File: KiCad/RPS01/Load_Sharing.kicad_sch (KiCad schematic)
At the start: 5 parts, among them U2 LTC4416EMS-1-TRPBF, U3 NP100P04PLG-E1-AY, U4 NP100P04PLG-E1-AY, U5 NP100P04PLG-E1-AY, U6 NP100P04PLG-E1-AY

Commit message: Updates
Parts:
- U2: footprint Mechatronic Footprints:MSOP-10_MS_LIT -> LTC4416:MSOP-10_MS_LIT
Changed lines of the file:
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@@
       (effects (font (size 1.524 1.524)))
     )
-    (property "Footprint" "Mechatronic Footprints:MSOP-10_MS_LIT" (at 91.44 119.38 0)
+    (property "Footprint" "LTC4416:MSOP-10_MS_LIT" (at 91.44 119.38 0)
       (effects (font (size 1.27 1.27) italic) hide)
     )

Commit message: Changed footprints on my end only
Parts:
- U2: footprint LTC4416:MSOP-10_MS_LIT -> Mechatronics LTC4416:MSOP-10_MS_LIT
- U3, U4, U5, U6: footprint Mechatronic Footprints:PRSS0004AL-A_REN -> Mechatronics LTC3780:PRSS0004AL-A_REN
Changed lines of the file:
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@@
       (effects (font (size 1.524 1.524)))
     )
-    (property "Footprint" "Mechatronic Footprints:PRSS0004AL-A_REN" (at 154.94 78.74 0)
+    (property "Footprint" "Mechatronics LTC3780:PRSS0004AL-A_REN" (at 154.94 78.74 0)
       (effects (font (size 1.27 1.27) italic) hide)
     )
@@
       (effects (font (size 1.524 1.524)))
     )
-    (property "Footprint" "LTC4416:MSOP-10_MS_LIT" (at 91.44 119.38 0)
+    (property "Footprint" "Mechatronics LTC4416:MSOP-10_MS_LIT" (at 91.44 119.38 0)
       (effects (font (size 1.27 1.27) italic) hide)
     )
@@
       (effects (font (size 1.524 1.524)))
     )
-    (property "Footprint" "Mechatronic Footprints:PRSS0004AL-A_REN" (at 154.94 50.8 0)
+    (property "Footprint" "Mechatronics LTC3780:PRSS0004AL-A_REN" (at 154.94 50.8 0)
       (effects (font (size 1.27 1.27) italic) hide)
     )
@@
       (effects (font (size 1.524 1.524)))
     )
-    (property "Footprint" "Mechatronic Footprints:PRSS0004AL-A_REN" (at 154.94 156.21 0)
+    (property "Footprint" "Mechatronics LTC3780:PRSS0004AL-A_REN" (at 154.94 156.21 0)
       (effects (font (size 1.27 1.27) italic) hide)
     )
@@
       (effects (font (size 1.524 1.524)))
     )
-    (property "Footprint" "Mechatronic Footprints:PRSS0004AL-A_REN" (at 154.94 130.81 0)
+    (property "Footprint" "Mechatronics LTC3780:PRSS0004AL-A_REN" (at 154.94 130.81 0)
       (effects (font (size 1.27 1.27) italic) hide)
     )

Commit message: All Footprints Load from Mechatronics Folder
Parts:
- U2: footprint Mechatronics LTC4416:MSOP-10_MS_LIT -> Mechatronic Footprints:LTC4416_MSOP-10_MS_LIT
- U3, U4, U5, U6: footprint Mechatronics LTC3780:PRSS0004AL-A_REN -> Mechatronic Footprints:LTC3780_PRSS0004AL-A_REN
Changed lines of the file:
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@@
       (effects (font (size 1.524 1.524)))
     )
-    (property "Footprint" "Mechatronics LTC3780:PRSS0004AL-A_REN" (at 154.94 78.74 0)
+    (property "Footprint" "Mechatronic Footprints:LTC3780_PRSS0004AL-A_REN" (at 154.94 78.74 0)
       (effects (font (size 1.27 1.27) italic) hide)
     )
@@
       (effects (font (size 1.524 1.524)))
     )
-    (property "Footprint" "Mechatronics LTC4416:MSOP-10_MS_LIT" (at 91.44 119.38 0)
+    (property "Footprint" "Mechatronic Footprints:LTC4416_MSOP-10_MS_LIT" (at 91.44 119.38 0)
       (effects (font (size 1.27 1.27) italic) hide)
     )
@@
       (effects (font (size 1.524 1.524)))
     )
-    (property "Footprint" "Mechatronics LTC3780:PRSS0004AL-A_REN" (at 154.94 50.8 0)
+    (property "Footprint" "Mechatronic Footprints:LTC3780_PRSS0004AL-A_REN" (at 154.94 50.8 0)
       (effects (font (size 1.27 1.27) italic) hide)
     )
@@
       (effects (font (size 1.524 1.524)))
     )
-    (property "Footprint" "Mechatronics LTC3780:PRSS0004AL-A_REN" (at 154.94 156.21 0)
+    (property "Footprint" "Mechatronic Footprints:LTC3780_PRSS0004AL-A_REN" (at 154.94 156.21 0)
       (effects (font (size 1.27 1.27) italic) hide)
     )
@@
       (effects (font (size 1.524 1.524)))
     )
-    (property "Footprint" "Mechatronics LTC3780:PRSS0004AL-A_REN" (at 154.94 130.81 0)
+    (property "Footprint" "Mechatronic Footprints:LTC3780_PRSS0004AL-A_REN" (at 154.94 130.81 0)
       (effects (font (size 1.27 1.27) italic) hide)
     )

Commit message: adjustments to main board revision
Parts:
- added U13, U8: NP100P04PLG-E1-AY, Mechatronic Footprints:LTC3780_PRSS0004AL-A_REN, symbol 2023-03-29_08-56-31:NP100P04PLG-E1-AY
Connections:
- net G1: now also U13.1 (GATE)
- net G2: now also U8.1 (GATE)
- net Vin1: now also U13.2 (DRAIN), U13.4 (FIN)
- net Vin2: now also U8.2 (DRAIN), U8.4 (FIN)
- net Vout: now also U13.3 (SOURCE), U8.3 (SOURCE)
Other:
- moved on the sheet: U2, U3, U4, U5, U6

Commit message: Updates
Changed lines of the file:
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@@
     (effects (font (size 1.27 1.27)) (justify left bottom))
   )
-  (label "VS" (at 157.48 104.14 0) (fields_autoplaced)
+  (label "+BATT" (at 157.48 104.14 0) (fields_autoplaced)
     (effects (font (size 1.27 1.27)) (justify left bottom))
   )

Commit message: Large Schematic Update
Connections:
- net Vin1 renamed VIN1
- net Vin2 renamed VIN2
- net Vout renamed VOUT
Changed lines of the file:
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@@
     (effects (font (size 1.27 1.27)) (justify left bottom))
   )
-  (hierarchical_label "Vout" (shape input) (at 167.64 104.14 0) (fields_autoplaced)
+  (hierarchical_label "VOUT" (shape input) (at 167.64 104.14 0) (fields_autoplaced)
     (effects (font (size 1.27 1.27)) (justify left))
   )
-  (hierarchical_label "Vin1" (shape input) (at 24.13 95.25 180) (fields_autoplaced)
+  (hierarchical_label "VIN1" (shape input) (at 24.13 95.25 180) (fields_autoplaced)
     (effects (font (size 1.27 1.27)) (justify right))
   )
-  (hierarchical_label "Vin2" (shape input) (at 22.86 111.76 180) (fields_autoplaced)
+  (hierarchical_label "VIN2" (shape input) (at 22.86 111.76 180) (fields_autoplaced)
     (effects (font (size 1.27 1.27)) (justify right))
   )

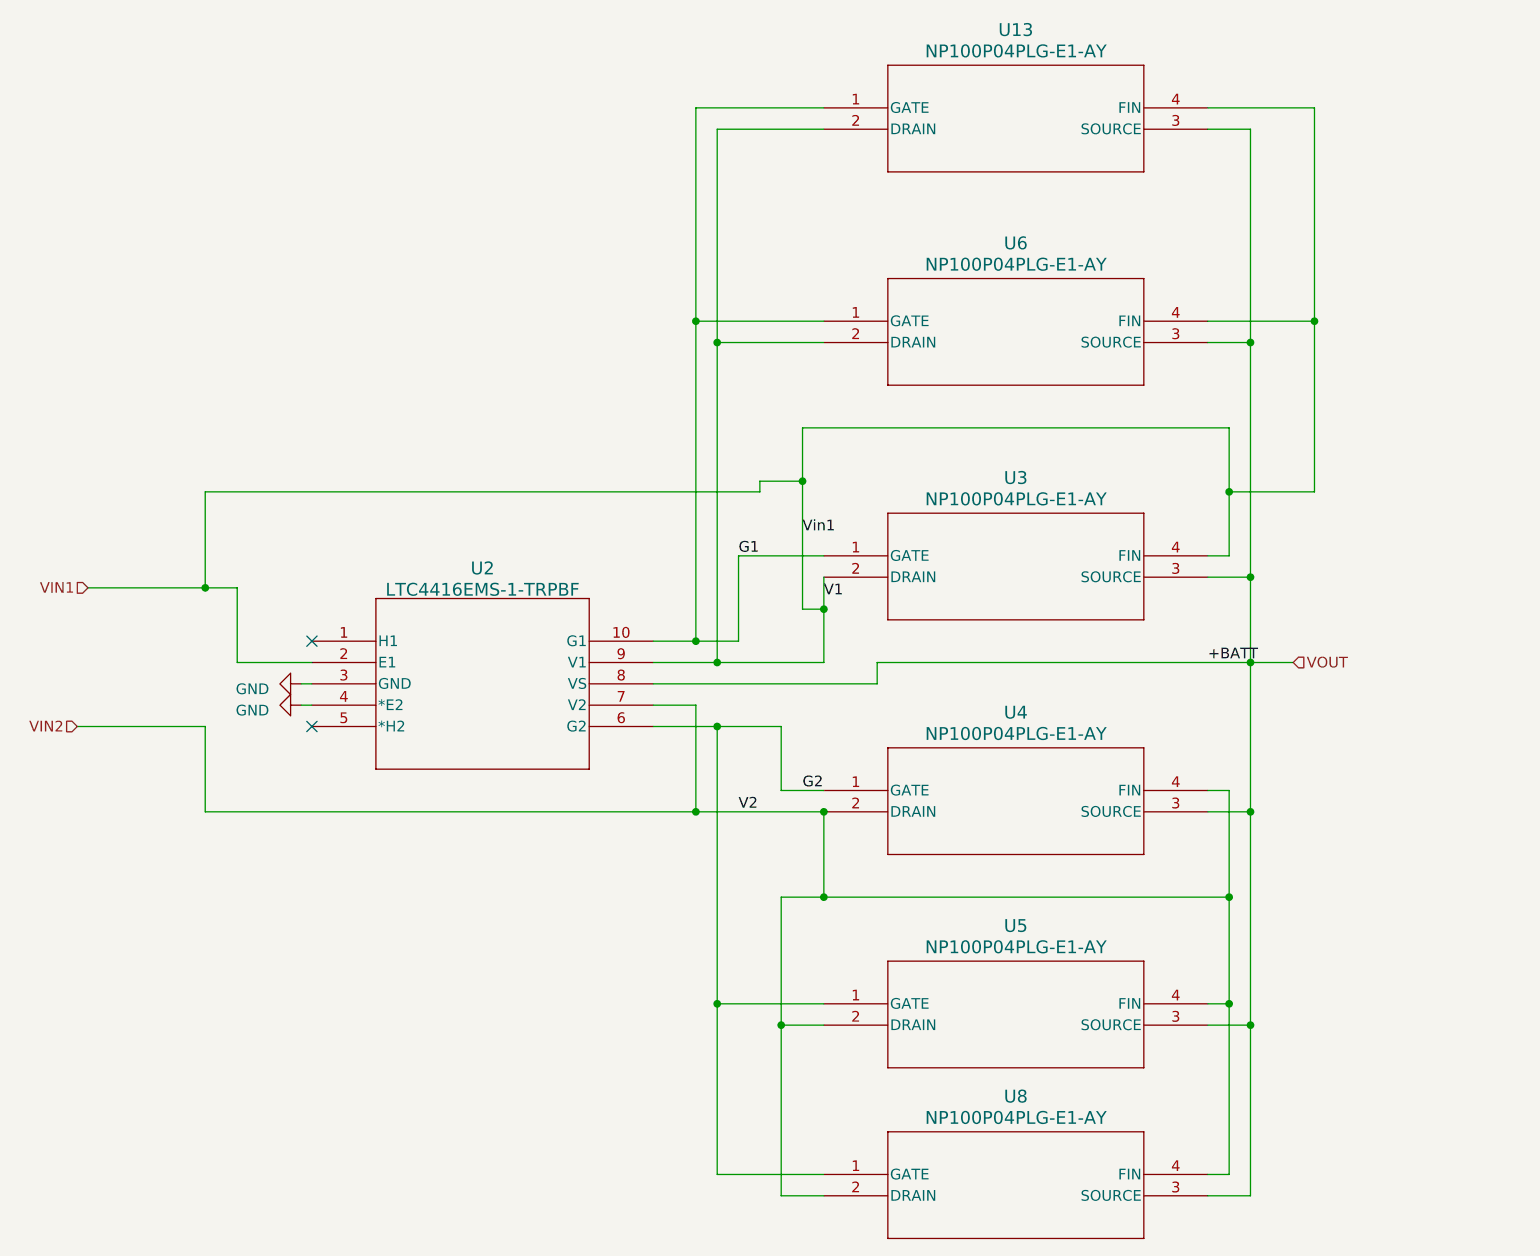
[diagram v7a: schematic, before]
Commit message: Finished most of the Schematics. Needs polishing
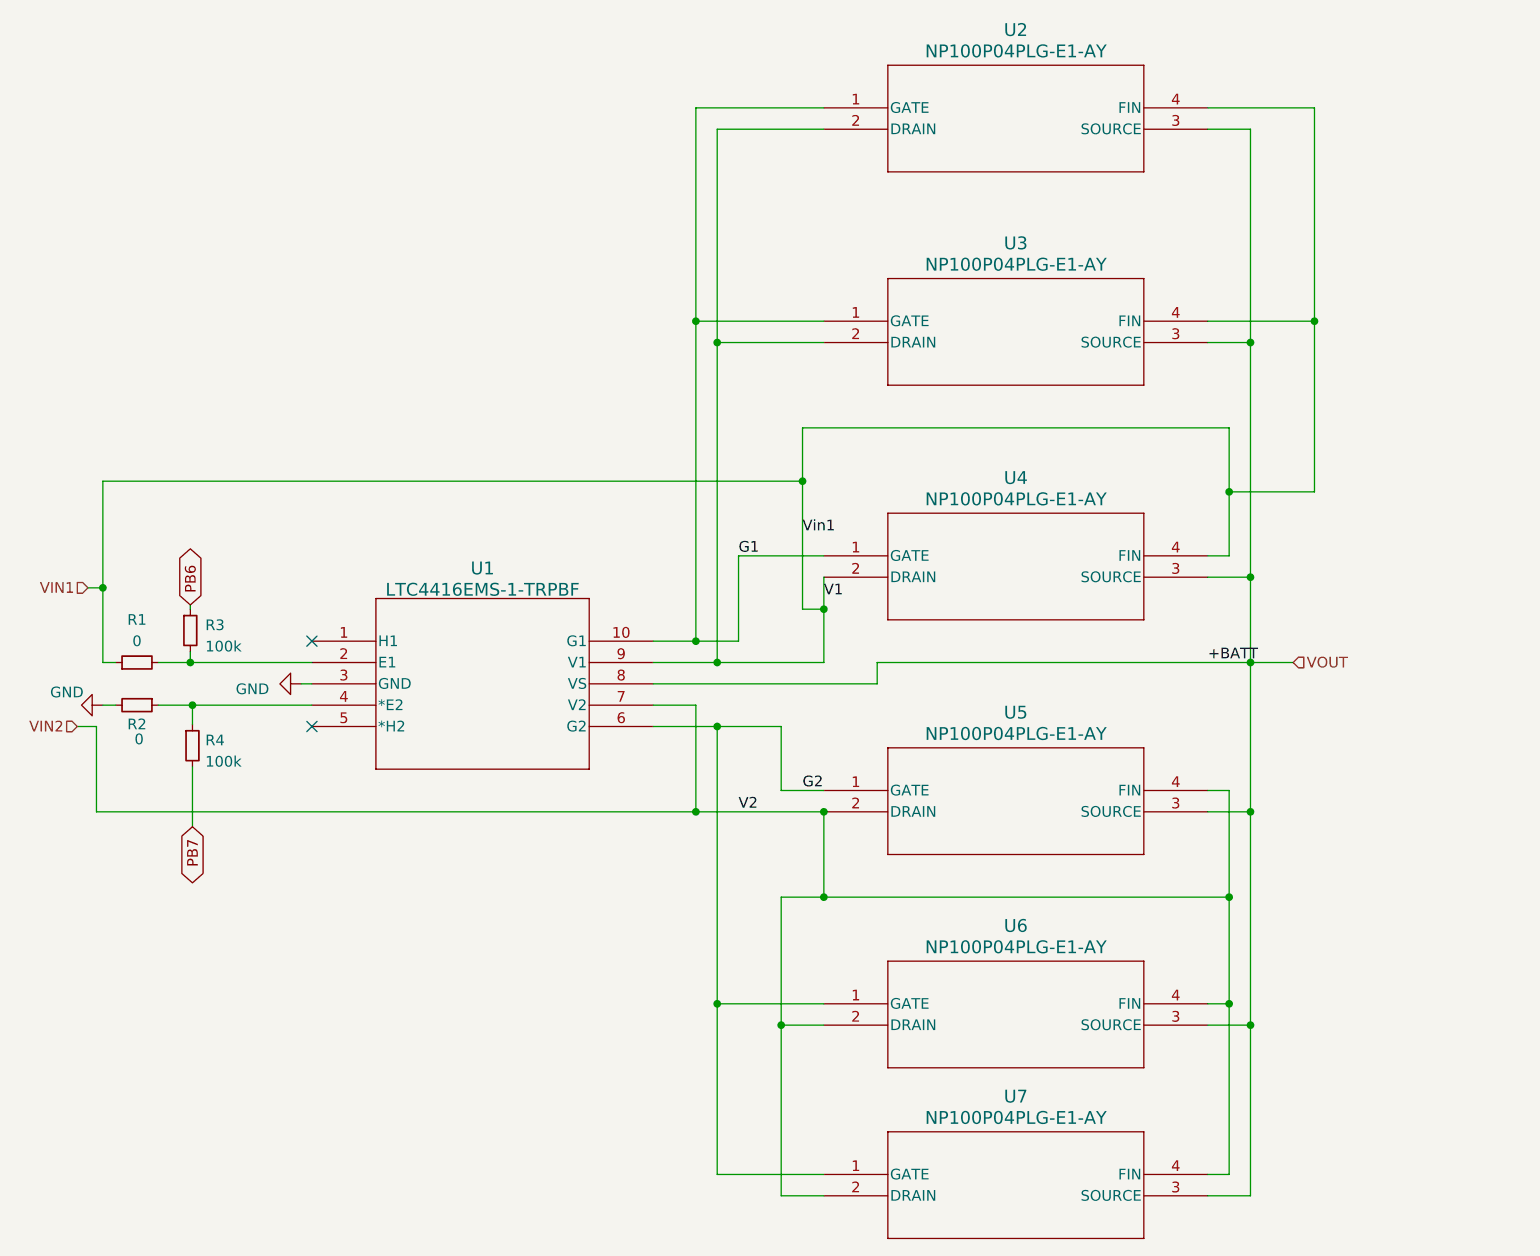
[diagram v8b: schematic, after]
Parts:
- added R1, R2: 0, symbol Device:R_Small
- added R3, R4: 100k, symbol Device:R_Small
- renumbered U2 to U1, U13 to U2, U6 to U3, U3 to U4, U4 to U5, U5 to U6, U8 to U7
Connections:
- net GND: now also R2.2; no longer U1.4 (*E2)
- net VIN1: now also R1.1; no longer U1.2 (E1)
- new net: R1.2, R3.2, U1.2 (E1)
- new net: R2.1, R4.1, U1.4 (*E2)
- new net PB6: R3.1
- new net PB7: R4.2
